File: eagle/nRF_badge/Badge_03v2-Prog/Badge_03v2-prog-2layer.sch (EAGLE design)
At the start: 4 parts, among them J1 PROG_CONN_6

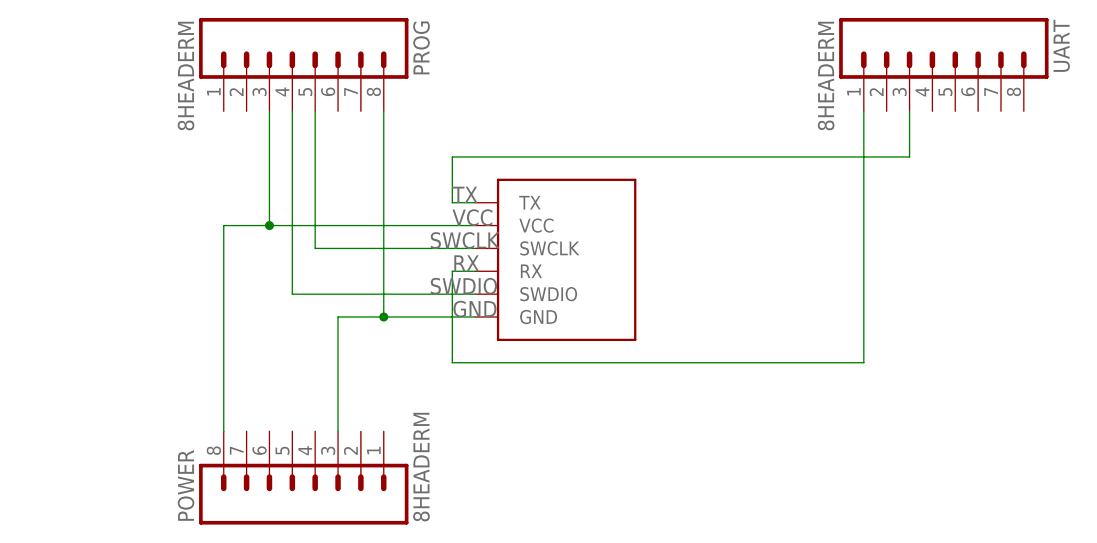
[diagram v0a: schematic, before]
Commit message: Added power LED to programmer. Gerber files
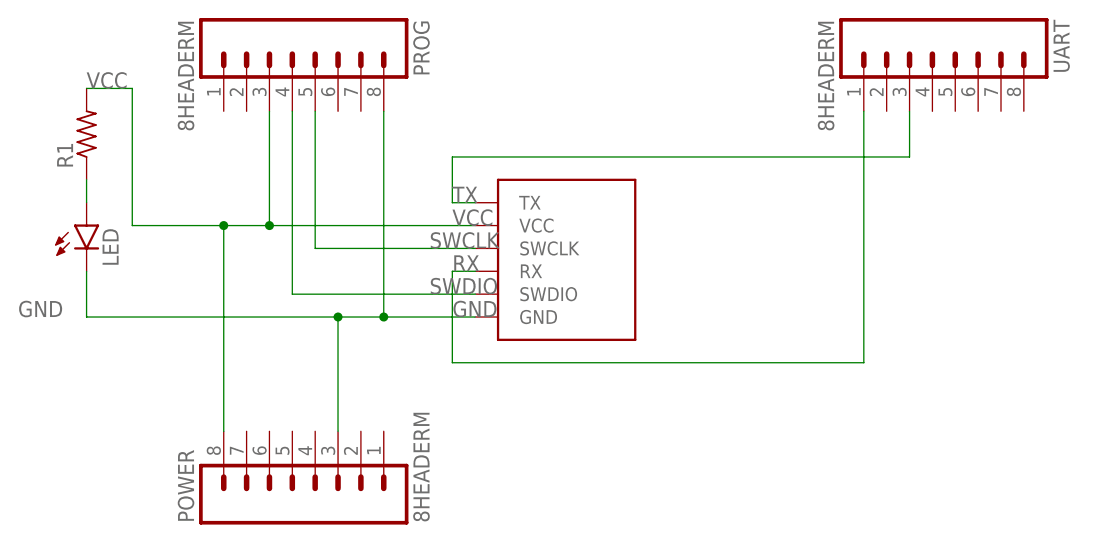
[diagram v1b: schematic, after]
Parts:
- added LED: (no value), Badge:LED
- added R1: (no value), rcl:R-US_R0603
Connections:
- new net N$1: LED.A, R1.1
- net GND: now also LED.C
- net VCC: now also R1.2
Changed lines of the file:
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@@
 <?xml version="1.0" encoding="utf-8"?>
 <!DOCTYPE eagle SYSTEM "eagle.dtd">
-<eagle version="7.4.0">
+<eagle version="7.7.0">
 <drawing>
 <settings>
@@
 <setting verticaltext="up"/>
 </settings>
-<grid distance="0.1" unitdist="inch" unit="inch" style="lines" multiple="1" display="yes" altdistance="0.01" altunitdist="inch" altunit="inch"/>
+<grid distance="0.1" unitdist="inch" unit="inch" style="lines" multiple="1" display="no" altdistance="0.01" altunitdist="inch" altunit="inch"/>
 <layers>
 <layer number="1" name="Top" color="4" fill="1" visible="no" active="no"/>
@@
 <part name="PROG" library="Badge" deviceset="8HEADER" device="M"/>
 <part name="UART" library="Badge" deviceset="8HEADER" device="M"/>
+<part name="LED" library="Badge" deviceset="LED" device=""/>
+<part name="R1" library="rcl" deviceset="R-US_" device="R0603"/>
 </parts>
 <sheets>
@@
 <instance part="PROG" gate="G$1" x="58.42" y="76.2" rot="R270"/>
 <instance part="UART" gate="G$1" x="129.54" y="76.2" rot="R270"/>
+<instance part="LED" gate="G$1" x="35.56" y="53.34"/>
+<instance part="R1" gate="G$1" x="35.56" y="66.04" rot="R90"/>
 </instances>
 <busses>
@@
 <wire x1="63.5" y1="45.72" x2="63.5" y2="33.02" width="0.1524" layer="91"/>
 <label x="76.2" y="45.72" size="1.778" layer="95"/>
+<pinref part="LED" gate="G$1" pin="C"/>
+<wire x1="35.56" y1="50.8" x2="35.56" y2="45.72" width="0.1524" layer="91"/>
+<wire x1="35.56" y1="45.72" x2="63.5" y2="45.72" width="0.1524" layer="91"/>
+<junction x="63.5" y="45.72"/>
+<label x="27.94" y="45.72" size="1.778" layer="95"/>
 </segment>
 </net>
@@
 <pinref part="J1" gate="G$1" pin="VCC"/>
 <label x="76.2" y="55.88" size="1.778" layer="95"/>
+<wire x1="50.8" y1="55.88" x2="40.64" y2="55.88" width="0.1524" layer="91"/>
+<wire x1="40.64" y1="55.88" x2="40.64" y2="71.12" width="0.1524" layer="91"/>
+<junction x="50.8" y="55.88"/>
+<pinref part="R1" gate="G$1" pin="2"/>
+<wire x1="40.64" y1="71.12" x2="35.56" y2="71.12" width="0.1524" layer="91"/>
+<label x="35.56" y="71.12" size="1.778" layer="95"/>
 </segment>
 </net>
@@
 </segment>
 </net>
+<net name="N$1" class="0">
+<segment>
+<pinref part="R1" gate="G$1" pin="1"/>
+<pinref part="LED" gate="G$1" pin="A"/>
+<wire x1="35.56" y1="60.96" x2="35.56" y2="58.42" width="0.1524" layer="91"/>
+</segment>
+</net>
